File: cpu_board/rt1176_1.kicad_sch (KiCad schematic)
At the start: 46 parts, among them SW1 SWITCH_SMT4.6X2.8, U2 MIMXRT1176

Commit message: add models and power diagram
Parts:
- U2, U? (x4): footprint adcs:BGA289C80P17X17_1400X14000X152 -> adcs:U_MIMXRT1176DVMAA_NXP
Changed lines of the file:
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@@
       (effects (font (size 1.27 1.27)))
     )
-    (property "Footprint" "adcs:BGA289C80P17X17_1400X14000X152" (at 223.52 67.31 0)
+    (property "Footprint" "adcs:U_MIMXRT1176DVMAA_NXP" (at 223.52 67.31 0)
       (effects (font (size 1.27 1.27)) hide)
     )
@@
       (effects (font (size 1.27 1.27)) hide)
     )
+    (property "DigiKey Part Number" "" (at 223.52 66.04 0)
+      (effects (font (size 1.27 1.27)) hide)
+    )
+    (property "Tolerance" "" (at 223.52 66.04 0)
+      (effects (font (size 1.27 1.27)))
+    )
+    (property "Power Rating" "" (at 223.52 66.04 0)
+      (effects (font (size 1.27 1.27)))
+    )
     (pin "L9")
     (pin "M10")
@@
       (effects (font (size 1.27 1.27)))
     )
-    (property "Footprint" "adcs:BGA289C80P17X17_1400X14000X152" (at 220.98 142.24 0)
+    (property "Footprint" "adcs:U_MIMXRT1176DVMAA_NXP" (at 220.98 142.24 0)
       (effects (font (size 1.27 1.27)) hide)
     )
@@
       (effects (font (size 1.27 1.27)) hide)
     )
+    (property "DigiKey Part Number" "" (at 220.98 140.97 0)
+      (effects (font (size 1.27 1.27)) hide)
+    )
+    (property "Tolerance" "" (at 220.98 140.97 0)
+      (effects (font (size 1.27 1.27)))
+    )
+    (property "Power Rating" "" (at 220.98 140.97 0)
+      (effects (font (size 1.27 1.27)))
+    )
     (pin "L9")
     (pin "M10")
@@
       (effects (font (size 1.27 1.27)))
     )
-    (property "Footprint" "adcs:BGA289C80P17X17_1400X14000X152" (at 50.8 240.03 0)
+    (property "Footprint" "adcs:U_MIMXRT1176DVMAA_NXP" (at 50.8 240.03 0)
       (effects (font (size 1.27 1.27)) hide)
     )
@@
       (effects (font (size 1.27 1.27)) hide)
     )
+    (property "DigiKey Part Number" "" (at 50.8 238.76 0)
+      (effects (font (size 1.27 1.27)) hide)
+    )
+    (property "Tolerance" "" (at 50.8 238.76 0)
+      (effects (font (size 1.27 1.27)))
+    )
+    (property "Power Rating" "" (at 50.8 238.76 0)
+      (effects (font (size 1.27 1.27)))
+    )
     (pin "L9")
     (pin "M10")
@@
       (effects (font (size 1.27 1.27)))
     )
-    (property "Footprint" "adcs:BGA289C80P17X17_1400X14000X152" (at 220.98 200.66 0)
+    (property "Footprint" "adcs:U_MIMXRT1176DVMAA_NXP" (at 220.98 200.66 0)
       (effects (font (size 1.27 1.27)) hide)
     )
@@
       (effects (font (size 1.27 1.27)) hide)
     )
+    (property "DigiKey Part Number" "" (at 220.98 199.39 0)
+      (effects (font (size 1.27 1.27)) hide)
+    )
+    (property "Tolerance" "" (at 220.98 199.39 0)
+      (effects (font (size 1.27 1.27)))
+    )
+    (property "Power Rating" "" (at 220.98 199.39 0)
+      (effects (font (size 1.27 1.27)))
+    )
     (pin "L9")
     (pin "M10")
@@
       (effects (font (size 1.27 1.27)))
     )
-    (property "Footprint" "adcs:BGA289C80P17X17_1400X14000X152" (at 219.71 255.27 0)
+    (property "Footprint" "adcs:U_MIMXRT1176DVMAA_NXP" (at 219.71 255.27 0)
       (effects (font (size 1.27 1.27)) hide)
     )
@@
       (effects (font (size 1.27 1.27)) hide)
     )
+    (property "DigiKey Part Number" "" (at 219.71 254 0)
+      (effects (font (size 1.27 1.27)) hide)
+    )
+    (property "Tolerance" "" (at 219.71 254 0)
+      (effects (font (size 1.27 1.27)))
+    )
+    (property "Power Rating" "" (at 219.71 254 0)
+      (effects (font (size 1.27 1.27)))
+    )
     (pin "L9")

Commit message: continue work on fanout
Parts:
- removed C?: 1uF, Capacitor_SMD:C_0402_1005Metric, symbol Device:C_Small
- removed D?: CDBQR00340-HF, adcs:D0402_H0.55MM, symbol Device:D_Schottky
- removed R?: 4k, Resistor_SMD:R_0402_1005Metric, symbol Device:R_US
- removed R?: 6.9k, Resistor_SMD:R_0402_1005Metric, symbol Device:R_US
- removed U?: TPS7A4501DCQT, mainboard:TPS7A4501DCQT, symbol mainboard:TPS7A4501DCQT
- added C?: 1uF, adcs:Perfect_0201, symbol Device:C_Small
- added R5: 2.2MΩ, adcs:Perfect_0402, symbol Device:R_Small_US
- added R6: 1.27MΩ, adcs:Perfect_0402, symbol Device:R_Small_US
- added U9: LT3014IS5-TRMPBF, adcs:S_5_ADI, symbol adcs:LT3014IS5-TRMPBF
- C10, C12, C13, C14, C15, C23, C26, C31, C34, C38, C40, C41, C42, C43, C8, C? (x3): footprint Capacitor_SMD:C_0402_1005Metric -> adcs:Perfect_0201
- C17, C22, C9: footprint Capacitor_SMD:C_0402_1005Metric -> adcs:Perfect_0201; Footprint (for JLCPCB) 0402 -> 0201
- C4, C? (x4): footprint Capacitor_SMD:C_0402_1005Metric -> adcs:Perfect_0402
- C6: footprint Capacitor_SMD:C_0402_1005Metric -> adcs:Perfect_0201; Footprint (for JLCPCB) 0402 -> 0201; Voltage Rating (none) -> 6.3V
- FB1, FB2: footprint Inductor_SMD:L_0402_1005Metric -> adcs:Perfect_0402
- R7, R8: footprint Resistor_SMD:R_0402_1005Metric -> adcs:Perfect_0402
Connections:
- net GND: now also C?.1, R6.1, U9.2 (GND)
- net VDD_SNVS_3V3: now also C?.2, R5.2, U9.5 (OUT)
- net VSYS: now also U9.1 (IN), U9.3 (*SHDN)
- new net: R5.1, R6.2, U9.4 (ADJ)
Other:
- note added: "1.22 * (1 + 2.2 / 1.27) + 0.000004 * 2.2 = 3.33V"
- moved on the sheet: C14, C8, C?

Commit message: grounded
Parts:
- C31, C? (x2): footprint adcs:Perfect_0201 -> adcs:Perfect_0402
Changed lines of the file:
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@@
       (effects (font (size 1.27 1.27)) (justify left))
     )
-    (property "Footprint" "adcs:Perfect_0201" (at 270.51 50.8 0)
+    (property "Footprint" "adcs:Perfect_0402" (at 270.51 50.8 0)
       (effects (font (size 1.27 1.27)) hide)
     )
@@
     (property "Footprint (for JLCPCB)" "0402" (at 270.51 50.8 0)
       (effects (font (size 1.27 1.27)) hide)
+    )
+    (property "DigiKey Part Number" "" (at 270.51 50.8 0)
+      (effects (font (size 1.27 1.27)) hide)
+    )
+    (property "Tolerance" "" (at 270.51 50.8 0)
+      (effects (font (size 1.27 1.27)))
+    )
+    (property "Power Rating" "" (at 270.51 50.8 0)
+      (effects (font (size 1.27 1.27)))
     )
     (pin "1")
@@
       (effects (font (size 1.27 1.27)) (justify left))
     )
-    (property "Footprint" "adcs:Perfect_0201" (at 53.975 43.815 0)
+    (property "Footprint" "adcs:Perfect_0402" (at 53.975 43.815 0)
       (effects (font (size 1.27 1.27)) hide)
     )
@@
     (property "Footprint (for JLCPCB)" "0402" (at 53.975 43.815 0)
       (effects (font (size 1.27 1.27)) hide)
+    )
+    (property "DigiKey Part Number" "" (at 53.975 43.815 0)
+      (effects (font (size 1.27 1.27)) hide)
+    )
+    (property "Tolerance" "" (at 53.975 43.815 0)
+      (effects (font (size 1.27 1.27)))
+    )
+    (property "Power Rating" "" (at 53.975 43.815 0)
+      (effects (font (size 1.27 1.27)))
     )
     (pin "1")
@@
       (effects (font (size 1.27 1.27)) (justify left))
     )
-    (property "Footprint" "adcs:Perfect_0201" (at 123.19 38.1 0)
-      (effects (font (size 1.27 1.27)) hide)
-    )
+    (property "Footprint" "adcs:Perfect_0402" (at 123.19 38.1 0)
+      (effects (font (size 1.27 1.27)) hide)
+    )

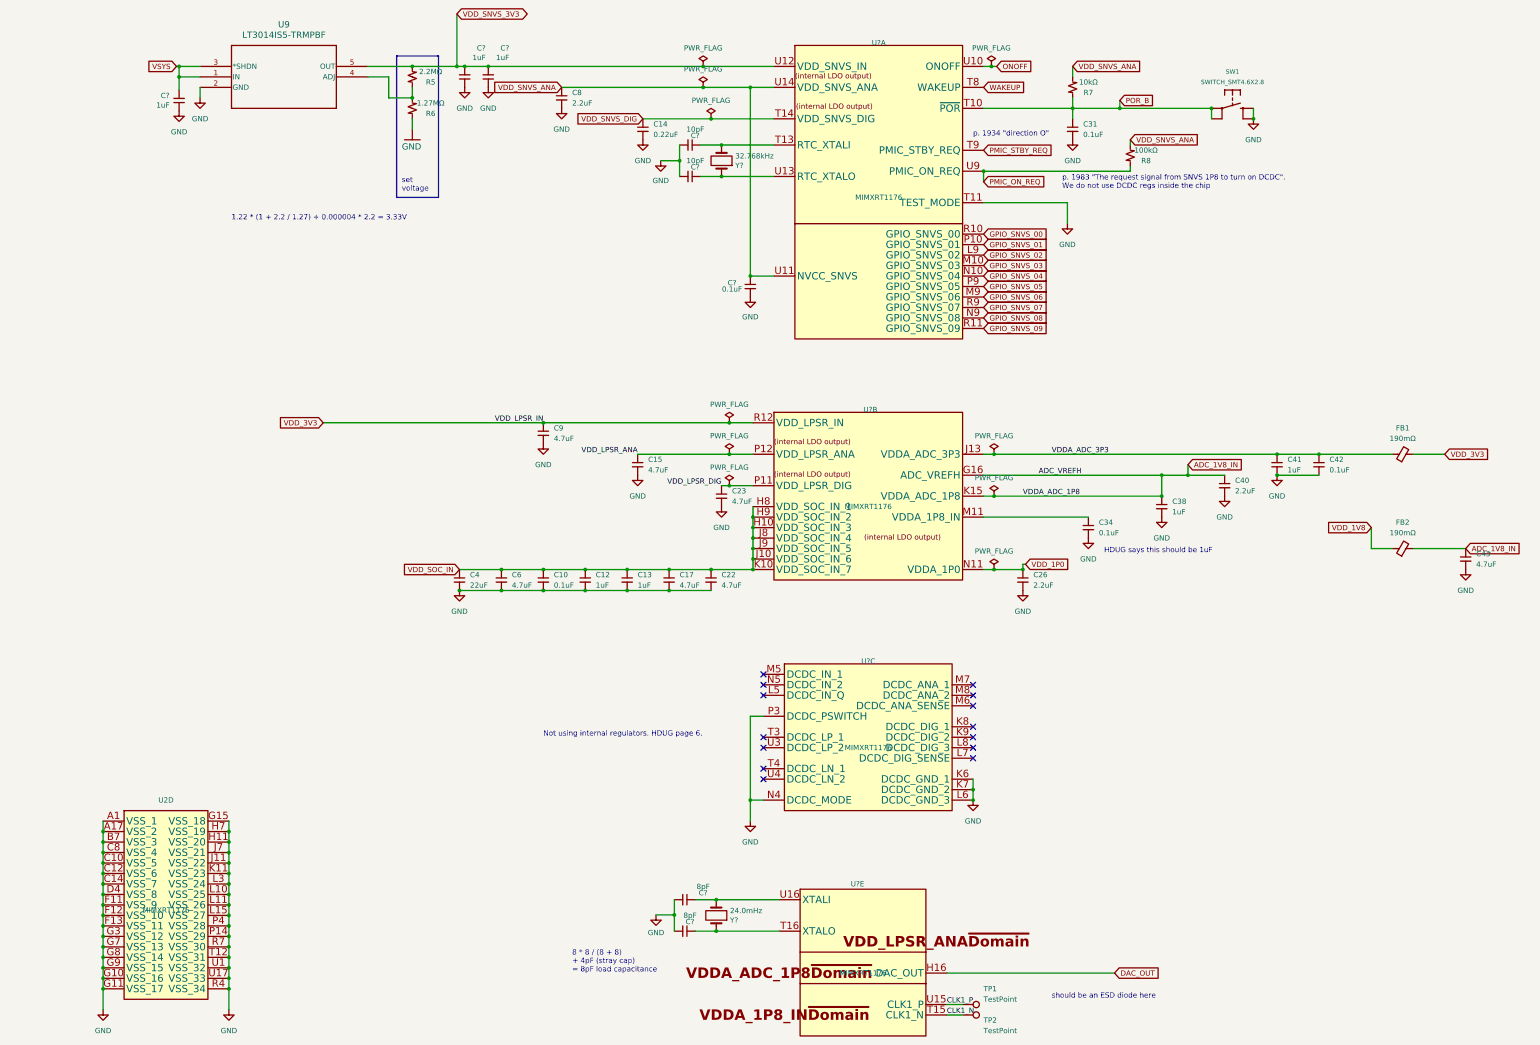
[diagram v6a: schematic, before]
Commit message: add load switch
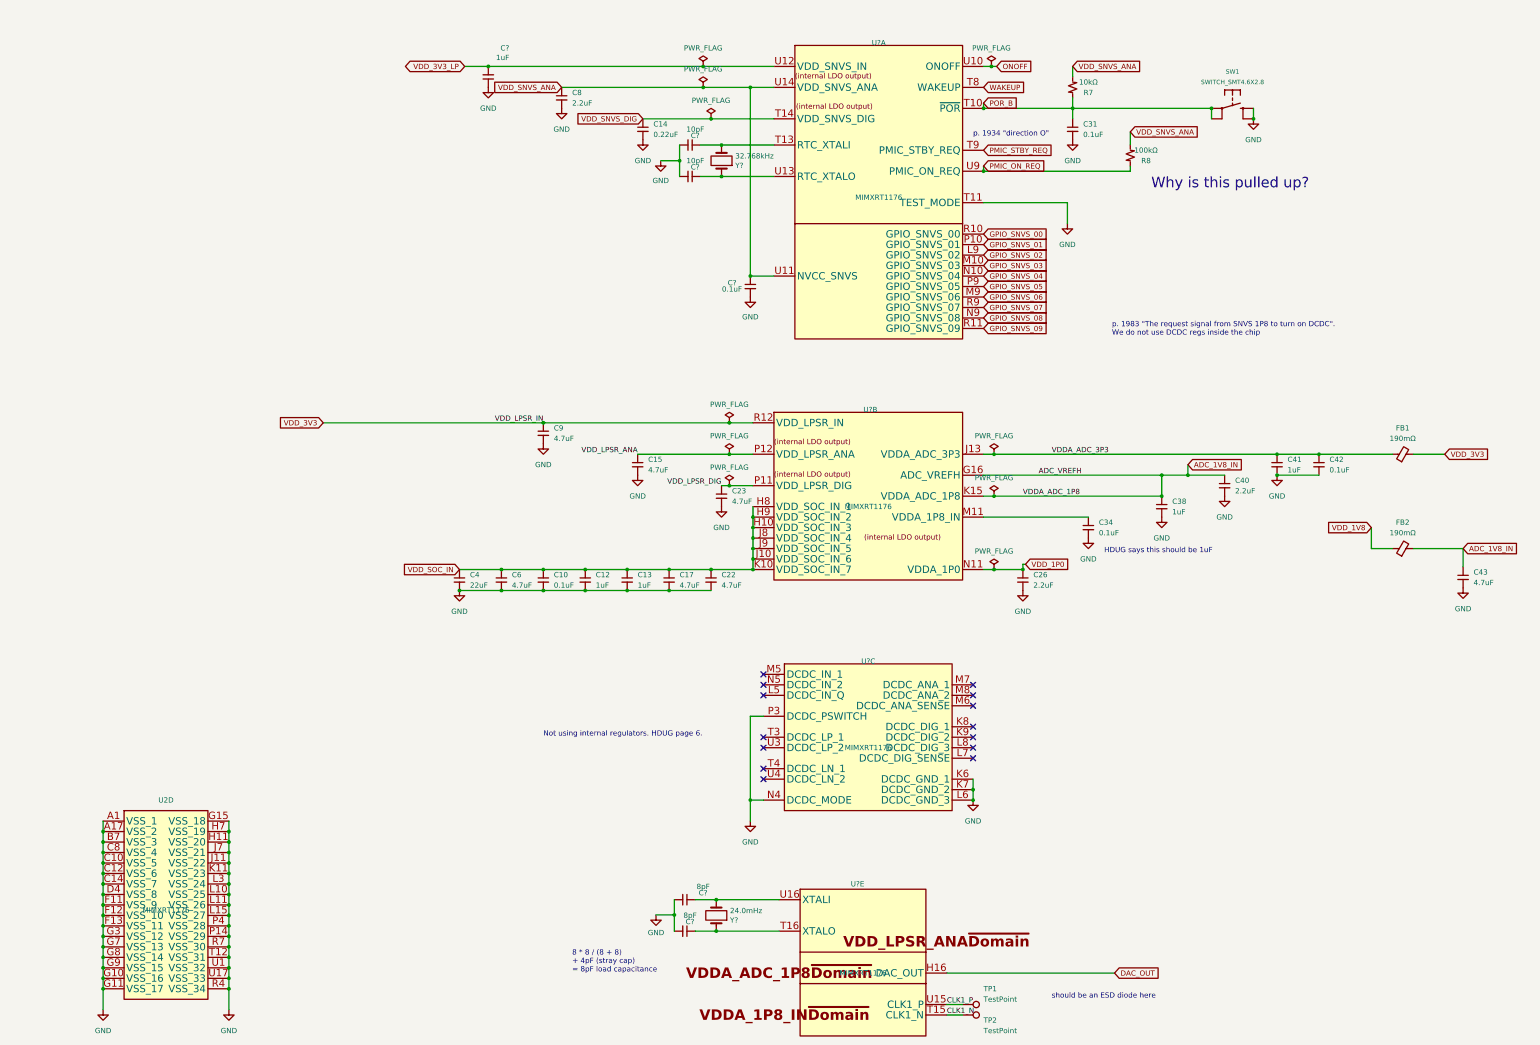
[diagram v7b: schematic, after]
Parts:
- removed C? (x2): 1uF, adcs:Perfect_0402, symbol Device:C_Small
- removed R5: 2.2MΩ, adcs:Perfect_0402, symbol Device:R_Small_US
- removed R6: 1.27MΩ, adcs:Perfect_0402, symbol Device:R_Small_US
- removed U9: LT3014IS5-TRMPBF, adcs:S_5_ADI, symbol adcs:LT3014IS5-TRMPBF
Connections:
- net VDD_SNVS_3V3 renamed VDD_3V3_LP
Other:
- note added: "Why is this pulled up?"
- note removed: "1.22 * (1 + 2.2 / 1.27) + 0.000004 * 2.2 = 3.33V"
- note removed: "set voltage"
- moved on the sheet: C43
